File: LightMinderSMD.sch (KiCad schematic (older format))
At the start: 31 parts, among them IC2 VN750PSTR-E, J1 Conn_01x06_Male, J3 Conn_01x03, Q1 Q_NPN_BCE, U2 LP2951-5.0_SOIC

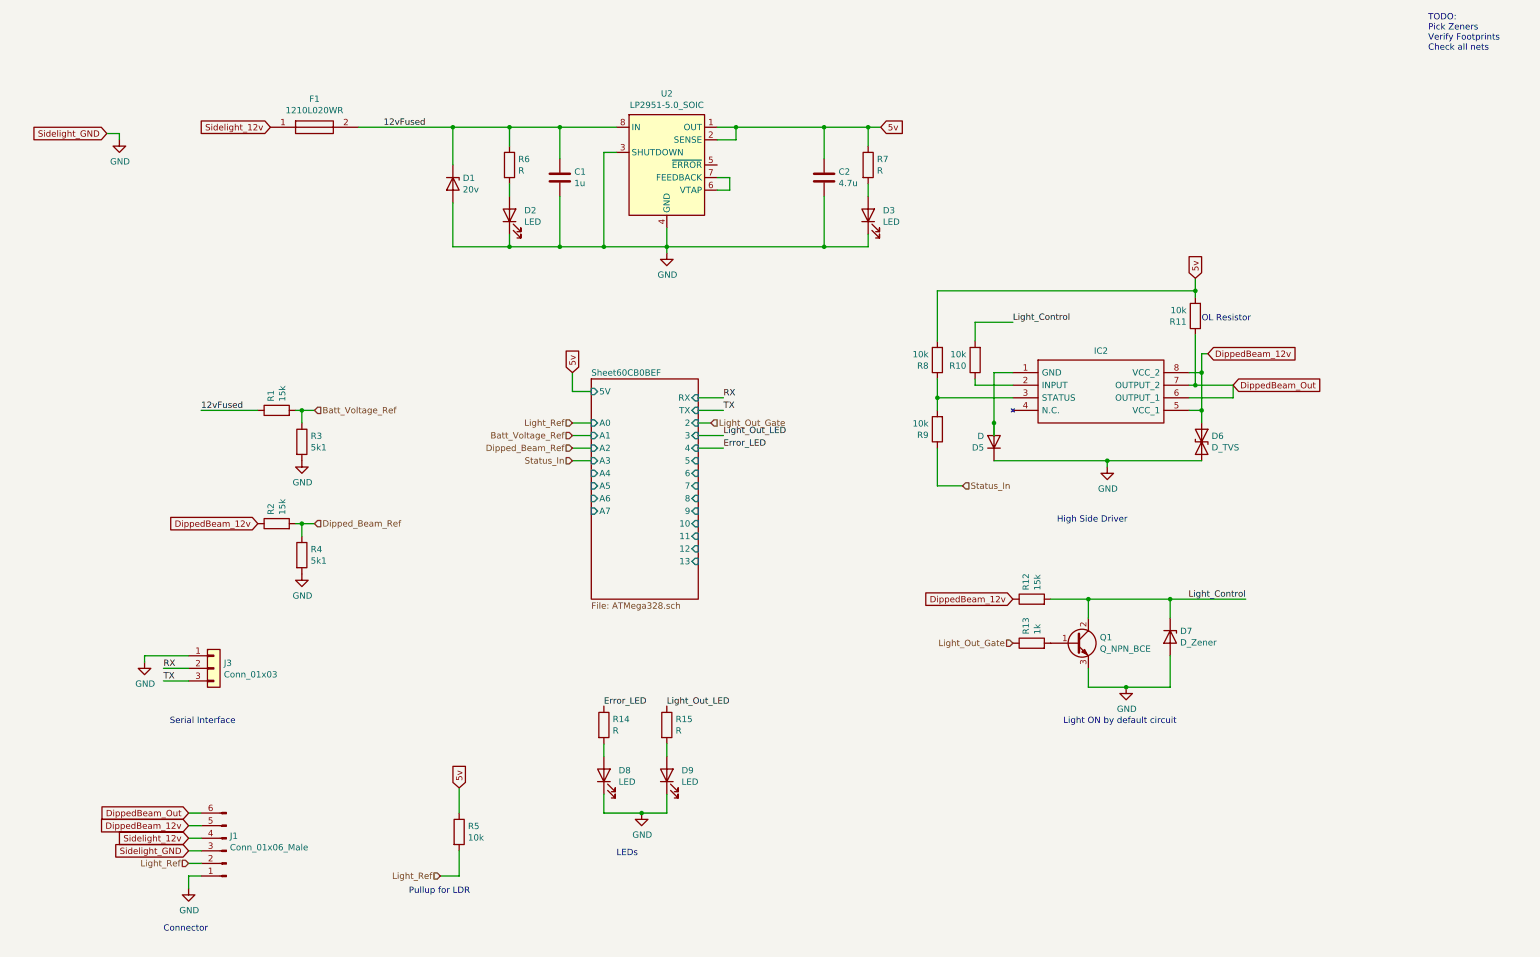
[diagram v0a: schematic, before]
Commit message: Version 2 PCB fully routed, simulations added
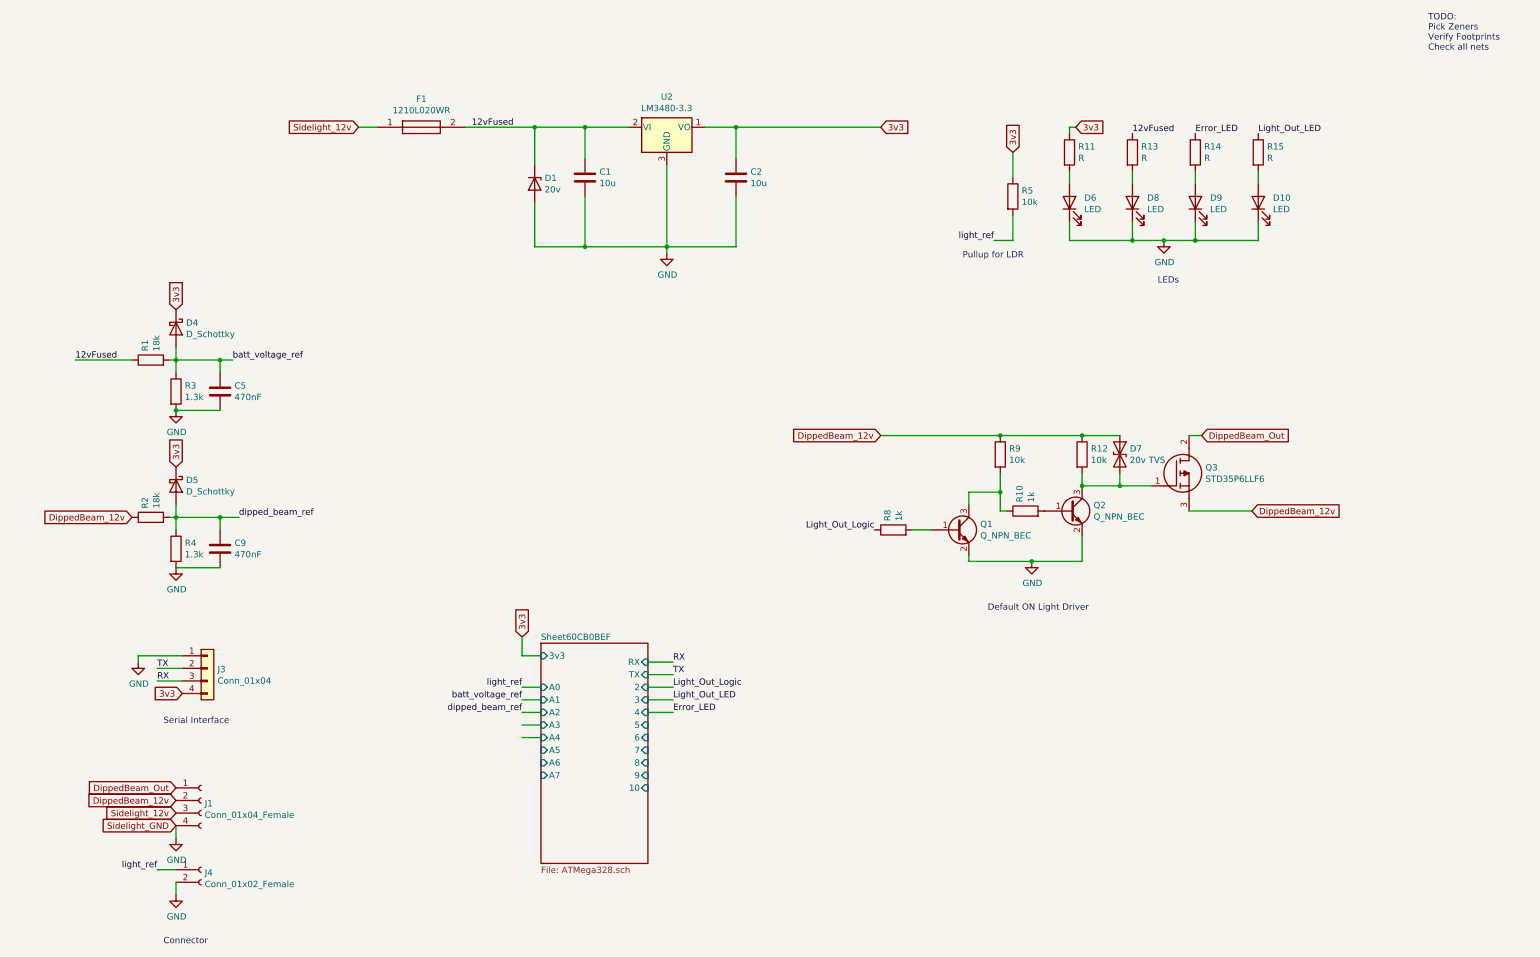
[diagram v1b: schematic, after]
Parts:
- removed D2, D3: LED, LED_SMD:LED_0805_2012Metric_Castellated, symbol Device:LED
- removed D5: D, Diode_SMD:D_0603_1608Metric, symbol Device:D
- removed D6: D_TVS, Diode_SMD:D_SOT-23_NKA, symbol Device:D_TVS
- removed D7: D_Zener, Diode_SMD:D_SOD-323F, symbol Device:D_Zener
- removed IC2: VN750PSTR-E, SOIC127P600X175-8N, symbol SamacSys_Parts:VN750PSTR-E
- removed J1: Conn_01x06_Male, Connector_PinHeader_2.54mm:PinHeader_1x06_P2.54mm_Vertical, symbol Connector:Conn_01x06_Male
- removed J3: Conn_01x03, Connector_PinHeader_2.54mm:PinHeader_1x03_P2.54mm_Vertical, symbol Connector_Generic:Conn_01x03
- removed Q1: Q_NPN_BCE, Package_TO_SOT_SMD:SOT-23, symbol Device:Q_NPN_BCE
- removed R6, R7: R, Resistor_SMD:R_0201_0603Metric, symbol Device:R
- removed U2: LP2951-5.0_SOIC, Package_SO:SOIC-8_3.9x4.9mm_P1.27mm, symbol Regulator_Linear:LP2951-5.0_SOIC
- added C5, C9: 470nF, Capacitor_SMD:C_0201_0603Metric, symbol Device:C
- added D10, D6: LED, LED_SMD:LED_0805_2012Metric_Castellated, symbol Device:LED
- added D4, D5: D_Schottky, Diode_SMD:D_SOT-23_ANK, symbol Device:D_Schottky
- added D7: 20v TVS, SamacSys_Parts:DO-214ACSMA, symbol Device:D_TVS
- added J1: Conn_01x04_Female, Connector_PinHeader_2.54mm:PinHeader_1x04_P2.54mm_Vertical, symbol Connector:Conn_01x04_Female
- added J3: Conn_01x04, Connector_PinHeader_2.54mm:PinHeader_1x04_P2.54mm_Vertical, symbol Connector_Generic:Conn_01x04
- added J4: Conn_01x02_Female, Connector_PinHeader_2.54mm:PinHeader_1x02_P2.54mm_Vertical, symbol Connector:Conn_01x02_Female
- added Q1, Q2: Q_NPN_BEC, SamacSys_Parts:SOT95P240X115-3N, symbol Device:Q_NPN_BEC
- added Q3: STD35P6LLF6, STD35P6LLF6, symbol SamacSys_Parts:STD35P6LLF6
- added U2: LM3480-3.3, Package_TO_SOT_SMD:SOT-23, symbol Regulator_Linear:LM3480-3.3
- C1: value 1u -> 10u
- C2: value 4.7u -> 10u
- R1, R2: value 15k -> 18k
- R10, R8: value 10k -> 1k; footprint Resistor_SMD:R_0201_0603Metric -> Resistor_SMD:R_0402_1005Metric; LSCS (none) -> C11702
- R11: value 10k -> R
- R12: value 15k -> 10k; footprint Resistor_SMD:R_0201_0603Metric -> Resistor_SMD:R_0402_1005Metric; LSCS (none) -> C25744
- R13: value 1k -> R
- R3, R4: value 5k1 -> 1.3k
- R9: footprint Resistor_SMD:R_0201_0603Metric -> Resistor_SMD:R_0402_1005Metric; LSCS (none) -> C25744
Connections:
- net Light_Out_Gate is gone; now on net 12vFused: R13.1
- net Status_In is gone; now on net DippedBeam_12v: R9.1
- net 12vFused: now also U2.2 (VI)
- net DippedBeam_12v: now also D7.1 (A1), J1.2 (Pin_2), Q3.3
- net DippedBeam_Out: now also J1.1 (Pin_1), Q3.2; no longer R11.1
- net GND: now also C5.2, C9.2, D10.1 (K), D6.1 (K), J1.4 (Pin_4), J3.1 (Pin_1), J4.2 (Pin_2), Q1.2 (E), Q2.2 (E), U2.3 (GND)
- net RX: now also J3.3 (Pin_3)
- net Sidelight_12v: now also J1.3 (Pin_3)
- net TX: now also J3.2 (Pin_2)
- net at R10.1: now also R9.2, Q1.3 (C)
- net Light_Out_Logic: now reaches R8.1
- net Light_Out_Logic: no longer R9.2
- net at R13.2: now also D8.2 (A)
- net at R14.2: now also D9.2 (A); no longer D8.2 (A)
- net at R15.2: now also D10.2 (A); no longer D9.2 (A)
- net 5v renamed 3v3
- net 3v3: now also R11.1, D4.1 (K), D5.1 (K), J3.4 (Pin_4), U2.1 (VO); no longer R11.2, R8.2
- net Batt_Voltage_Ref renamed batt_voltage_ref
- net batt_voltage_ref: now also C5.1, D4.2 (A)
- net Dipped_Beam_Ref renamed dipped_beam_ref
- net dipped_beam_ref: now also C9.1, D5.2 (A)
- net Light_Control: no longer names the net of R10.2
- net Light_Control: now also Q2.1 (B); no longer R12.2
- net Light_Ref renamed light_ref
- net light_ref: now also J4.1 (Pin_1)
- new net: Q1.1 (B), R8.2
- new net: D7.2 (A2), Q2.3 (C), Q3.1, R12.2
- new net: D6.2 (A), R11.2
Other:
- note added: "Default ON Light Driver"
- note removed: "High Side Driver"
- note removed: "Light ON by default circuit"
- note removed: "OL Resistor"
- moved on the sheet: C1, C2, D1, R1, R3, R4

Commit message: Finalise PCB, add logo and silk text
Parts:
- R11, R14, R15: value R -> 100
- R13: value R -> 750
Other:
- note added: "Battery Voltage Step down to 1.1v"
- note added: "Dipped Beam Req Step down to 1.1v"
- moved on the sheet: C5, D4, R1, R3
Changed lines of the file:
@@
 L Device:R R1
 U 1 1 60C32AF5
-P 1700 2800
-F 0 "R1" H 1770 2846 50  0000 L CNN
-F 1 "18k" H 1770 2755 50  0000 L CNN
-F 2 "Resistor_SMD:R_0201_0603Metric" V 1630 2800 50  0001 C CNN
-F 3 "~" H 1700 2800 50  0001 C CNN
-	1    1700 2800
+P 1700 2350
+F 0 "R1" H 1770 2396 50  0000 L CNN
+F 1 "18k" H 1770 2305 50  0000 L CNN
+F 2 "Resistor_SMD:R_0201_0603Metric" V 1630 2350 50  0001 C CNN
+F 3 "~" H 1700 2350 50  0001 C CNN
+	1    1700 2350
 	0    -1   -1   0
 $EndComp
@@
 L Device:R R3
 U 1 1 60C33423
-P 1900 3050
-F 0 "R3" H 1970 3096 50  0000 L CNN
-F 1 "1.3k" H 1970 3005 50  0000 L CNN
-F 2 "Resistor_SMD:R_0201_0603Metric" V 1830 3050 50  0001 C CNN
-F 3 "~" H 1900 3050 50  0001 C CNN
-	1    1900 3050
+P 1900 2600
+F 0 "R3" H 1970 2646 50  0000 L CNN
+F 1 "1.3k" H 1970 2555 50  0000 L CNN
+F 2 "Resistor_SMD:R_0201_0603Metric" V 1830 2600 50  0001 C CNN
+F 3 "~" H 1900 2600 50  0001 C CNN
+	1    1900 2600
 	1    0    0    -1
 $EndComp
@@
 $EndComp
 Wire Wire Line
-	1850 2800 1900 2800
-Wire Wire Line
-	1900 2800 1900 2900
+	1850 2350 1900 2350
+Wire Wire Line
+	1900 2350 1900 2450
 Wire Wire Line
 	1850 4050 1900 4050
@@
 L power:GND #PWR0102
 U 1 1 60C44517
-P 1900 3200
-F 0 "#PWR0102" H 1900 2950 50  0001 C CNN
-F 1 "GND" H 1905 3027 50  0000 C CNN
-F 2 "" H 1900 3200 50  0001 C CNN
-F 3 "" H 1900 3200 50  0001 C CNN
-	1    1900 3200
+P 1900 2750
+F 0 "#PWR0102" H 1900 2500 50  0001 C CNN
+F 1 "GND" H 1905 2577 50  0000 C CNN
+F 2 "" H 1900 2750 50  0001 C CNN
+F 3 "" H 1900 2750 50  0001 C CNN
+	1    1900 2750
 	1    0    0    -1
 $EndComp
@@
 DippedBeam_12v
 Connection ~ 1900 4050
-Connection ~ 1900 2800
+Connection ~ 1900 2350
 Text GLabel 8550 1150 1    50   Input ~ 0
 3v3
@@
 $EndComp
 $Sheet
-S 4800 5050 850  1750
+S 4450 3250 850  1750
 U 60CB0BF0
 F0 "Sheet60CB0BEF" 50
 F1 "ATMega328.sch" 50
-F2 "A0" I L 4800 5400 50
-F3 "A1" I L 4800 5500 50
-F4 "A2" I L 4800 5600 50
-F5 "A3" I L 4800 5700 50
-F6 "A4" I L 4800 5800 50
-F7 "A5" I L 4800 5900 50
-F8 "RX" I R 5650 5200 50
-F9 "TX" I R 5650 5300 50
-F10 "2" I R 5650 5400 50
-F11 "3" I R 5650 5500 50
-F12 "4" I R 5650 5600 50
-F13 "5" I R 5650 5700 50
-F14 "6" I R 5650 5800 50
-F15 "7" I R 5650 5900 50
-F16 "8" I R 5650 6000 50
-F17 "9" I R 5650 6100 50
-F18 "10" I R 5650 6200 50
-F22 "A6" I L 4800 6000 50
-F23 "A7" I L 4800 6100 50
-F24 "3v3" I L 4800 5150 50
+F2 "A0" I L 4450 3600 50
+F3 "A1" I L 4450 3700 50
+F4 "A2" I L 4450 3800 50
+F5 "A3" I L 4450 3900 50
+F6 "A4" I L 4450 4000 50
+F7 "A5" I L 4450 4100 50
+F8 "RX" I R 5300 3400 50
+F9 "TX" I R 5300 3500 50
+F10 "2" I R 5300 3600 50
+F11 "3" I R 5300 3700 50
+F12 "4" I R 5300 3800 50
+F13 "5" I R 5300 3900 50
+F14 "6" I R 5300 4000 50
+F15 "7" I R 5300 4100 50
+F16 "8" I R 5300 4200 50
+F17 "9" I R 5300 4300 50
+F18 "10" I R 5300 4400 50
+F22 "A6" I L 4450 4200 50
+F23 "A7" I L 4450 4300 50
+F24 "3v3" I L 4450 3350 50
 $EndSheet
 Text GLabel 7500 950  2    50   Input ~ 0
@@
 	5150 950  5150 1200
 Wire Wire Line
-	4650 5400 4800 5400
-Wire Wire Line
-	4650 5500 4800 5500
-Wire Wire Line
-	4650 5600 4800 5600
-Text GLabel 4650 5000 1    50   Input ~ 0
+	4300 3600 4450 3600
+Wire Wire Line
+	4300 3700 4450 3700
+Wire Wire Line
+	4300 3800 4450 3800
+Text GLabel 4300 3200 1    50   Input ~ 0
 3v3
 Wire Wire Line
-	4650 5000 4650 5150
-Wire Wire Line
-	4800 5150 4650 5150
-Text Label 5850 5300 0    50   ~ 0
+	4300 3200 4300 3350
+Wire Wire Line
+	4450 3350 4300 3350
+Text Label 5500 3500 0    50   ~ 0
 TX
-Text Label 5850 5200 0    50   ~ 0
+Text Label 5500 3400 0    50   ~ 0
 RX
 Wire Wire Line
-	5850 5200 5650 5200
-Wire Wire Line
-	5850 5300 5650 5300
+	5500 3400 5300 3400
+Wire Wire Line
+	5500 3500 5300 3500
 Wire Wire Line
 	6350 1900 6350 1500
@@
 Connection ~ 5150 1900
 Wire Wire Line
-	4650 5700 4800 5700
+	4300 3900 4450 3900
 Text Notes 8150 2000 0    50   ~ 0
 Pullup for LDR
@@
 Text Label 4250 950  0    50   ~ 0
 12vFused
-Text Label 1100 2800 0    50   ~ 0
+Text Label 1100 2350 0    50   ~ 0
 12vFused
 Wire Wire Line
-	1100 2800 1550 2800
+	1100 2350 1550 2350
 $Comp
 L Device:D_Zener D1
@@
 $EndComp
 Wire Wire Line
-	5650 5500 5850 5500
-Wire Wire Line
-	5650 5600 5850 5600
-Text Label 5850 5500 0    50   ~ 0
+	5300 3700 5500 3700
+Wire Wire Line
+	5300 3800 5500 3800
+Text Label 5500 3700 0    50   ~ 0
 Light_Out_LED
-Text Label 5850 5600 0    50   ~ 0
+Text Label 5500 3800 0    50   ~ 0
 Error_LED
 Text Label 1750 5350 0    50   ~ 0
@@
 AR Path="/618FD111" Ref="R13"  Part="1"
 F 0 "R13" H 9570 1196 50  0000 L CNN
-F 1 "R" H 9570 1105 50  0000 L CNN
+F 1 "750" H 9570 1105 50  0000 L CNN
 F 2 "Resistor_SMD:R_0201_0603Metric" V 9430 1150 50  0001 C CNN
 F 3 "~" H 9500 1150 50  0001 C CNN
@@
 AR Path="/618FD11E" Ref="R11"  Part="1"
 F 0 "R11" H 9070 1196 50  0000 L CNN
-F 1 "R" H 9070 1105 50  0000 L CNN
+F 1 "100" H 9070 1105 50  0000 L CNN
 F 2 "Resistor_SMD:R_0201_0603Metric" V 8930 1150 50  0001 C CNN
 F 3 "~" H 9000 1150 50  0001 C CNN
@@
 AR Path="/618FD12C" Ref="R14"  Part="1"
 F 0 "R14" H 10070 1196 50  0000 L CNN
-F 1 "R" H 10070 1105 50  0000 L CNN
+F 1 "100" H 10070 1105 50  0000 L CNN
 F 2 "Resistor_SMD:R_0201_0603Metric" V 9930 1150 50  0001 C CNN
 F 3 "~" H 10000 1150 50  0001 C CNN
@@
 AR Path="/618FD139" Ref="R15"  Part="1"
 F 0 "R15" H 10570 1196 50  0000 L CNN
-F 1 "R" H 10570 1105 50  0000 L CNN
+F 1 "100" H 10570 1105 50  0000 L CNN
 F 2 "Resistor_SMD:R_0201_0603Metric" V 10430 1150 50  0001 C CNN
 F 3 "~" H 10500 1150 50  0001 C CNN
@@
 	10000 1850 10500 1850
 Wire Wire Line
-	1900 2800 1900 2700
+	1900 2350 1900 2250
 Wire Wire Line
 	1900 4050 1900 3950
 Text GLabel 1900 3650 1    50   Input ~ 0
 3v3
-Text GLabel 1900 2400 1    50   Input ~ 0
+Text GLabel 1900 1950 1    50   Input ~ 0
 3v3
 $Comp
@@
 $EndComp
 Wire Wire Line
-	4800 5800 4650 5800
-Wire Wire Line
-	5650 5400 5850 5400
-Text Label 5850 5400 0    50   ~ 0
+	4450 4000 4300 4000
+Wire Wire Line
+	5300 3600 5500 3600
+Text Label 5500 3600 0    50   ~ 0
 Light_Out_Logic
 Text GLabel 7500 3400 0    50   Input ~ 0
@@
 L Device:D_Schottky D4
 U 1 1 61982702
-P 1900 2550
-F 0 "D4" V 1854 2630 50  0000 L CNN
-F 1 "D_Schottky" V 1945 2630 50  0000 L CNN
-F 2 "Diode_SMD:D_SOT-23_ANK" H 1900 2550 50  0001 C CNN
-F 3 "~" H 1900 2550 50  0001 C CNN
-	1    1900 2550
+P 1900 2100
+F 0 "D4" V 1854 2180 50  0000 L CNN
+F 1 "D_Schottky" V 1945 2180 50  0000 L CNN
+F 2 "Diode_SMD:D_SOT-23_ANK" H 1900 2100 50  0001 C CNN
+F 3 "~" H 1900 2100 50  0001 C CNN
+	1    1900 2100
 	0    1    1    0
 $EndComp
@@
 L Device:C C?
 U 1 1 6198C42D
-P 2250 3050
+P 2250 2600
 AR Path="/60CB0BF0/6198C42D" Ref="C?"  Part="1"
 AR Path="/6198C42D" Ref="C5"  Part="1"
-F 0 "C5" H 2365 3096 50  0000 L CNN
-F 1 "470nF" H 2365 3005 50  0000 L CNN
-F 2 "Capacitor_SMD:C_0201_0603Metric" H 2288 2900 50  0001 C CNN
-F 3 "~" H 2250 3050 50  0001 C CNN
-	1    2250 3050
-	1    0    0    -1
-$EndComp
-Wire Wire Line
-	2250 3200 1900 3200
+F 0 "C5" H 2365 2646 50  0000 L CNN
+F 1 "470nF" H 2365 2555 50  0000 L CNN
+F 2 "Capacitor_SMD:C_0201_0603Metric" H 2288 2450 50  0001 C CNN
+F 3 "~" H 2250 2600 50  0001 C CNN
+	1    2250 2600
+	1    0    0    -1
+$EndComp
+Wire Wire Line
+	2250 2750 1900 2750
 Wire Wire Line
 	1900 4050 2250 4050
@@
 Wire Wire Line
 	2250 4050 2400 4050
-Connection ~ 1900 3200
-Wire Wire Line
-	1900 2800 2250 2800
-Wire Wire Line
-	2250 2900 2250 2800
-Wire Wire Line
-	2250 2800 2350 2800
-Connection ~ 2250 2800
+Connection ~ 1900 2750
+Wire Wire Line
+	1900 2350 2250 2350
+Wire Wire Line
+	2250 2450 2250 2350
+Wire Wire Line
+	2250 2350 2350 2350
+Connection ~ 2250 2350
 $Comp
 L Device:C C?
@@
 Text Label 2400 4050 0    50   ~ 0
 dipped_beam_ref
-Text Label 2350 2800 0    50   ~ 0
+Text Label 2350 2350 0    50   ~ 0
 batt_voltage_ref
-Text Label 4650 5500 2    50   ~ 0
+Text Label 4300 3700 2    50   ~ 0
 batt_voltage_ref
-Text Label 4650 5600 2    50   ~ 0
+Text Label 4300 3800 2    50   ~ 0
 dipped_beam_ref
-Text Label 4650 5400 2    50   ~ 0
+Text Label 4300 3600 2    50   ~ 0
 light_ref
 Text Label 8400 1850 2    50   ~ 0
@@
 Wire Wire Line
 	1900 6850 1750 6850
+Text Notes 1250 3150 0    50   ~ 0
+Battery Voltage Step down to 1.1v
+Text Notes 1250 4850 0    50   ~ 0
+Dipped Beam Req Step down to 1.1v
 $EndSCHEMATC

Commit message: Version 0.3 prototype - Manufactured
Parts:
- removed D4, D5: D_Schottky, Diode_SMD:D_SOT-23_ANK, symbol Device:D_Schottky
- C5, C9: footprint Capacitor_SMD:C_0201_0603Metric -> Capacitor_SMD:C_0603_1608Metric
- F1: symbol SamacSys_Parts:1210L020WR -> LightMinderSMD-rescue:1210L020WR-SamacSys_Parts
- Q3: symbol SamacSys_Parts:STD35P6LLF6 -> LightMinderSMD-rescue:STD35P6LLF6-SamacSys_Parts
- R1, R11, R13, R14, R15, R2, R3, R4, R5: footprint Resistor_SMD:R_0201_0603Metric -> Resistor_SMD:R_0603_1608Metric
- R10, R12, R8, R9: footprint Resistor_SMD:R_0402_1005Metric -> Resistor_SMD:R_0603_1608Metric
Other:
- note added: "Analogue Input Circuits"
- note added: "External Connectors"
- note added: "LEDs and LDR Pullup"
- note added: "Power Supply"
- note removed: "LEDs"
- moved on the sheet: C1, C2, C5, C9, D1, D10, D6, D7, D8, D9, F1, J1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
